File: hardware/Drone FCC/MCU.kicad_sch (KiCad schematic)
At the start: 11 parts, among them U3 STM32F746ZGTx

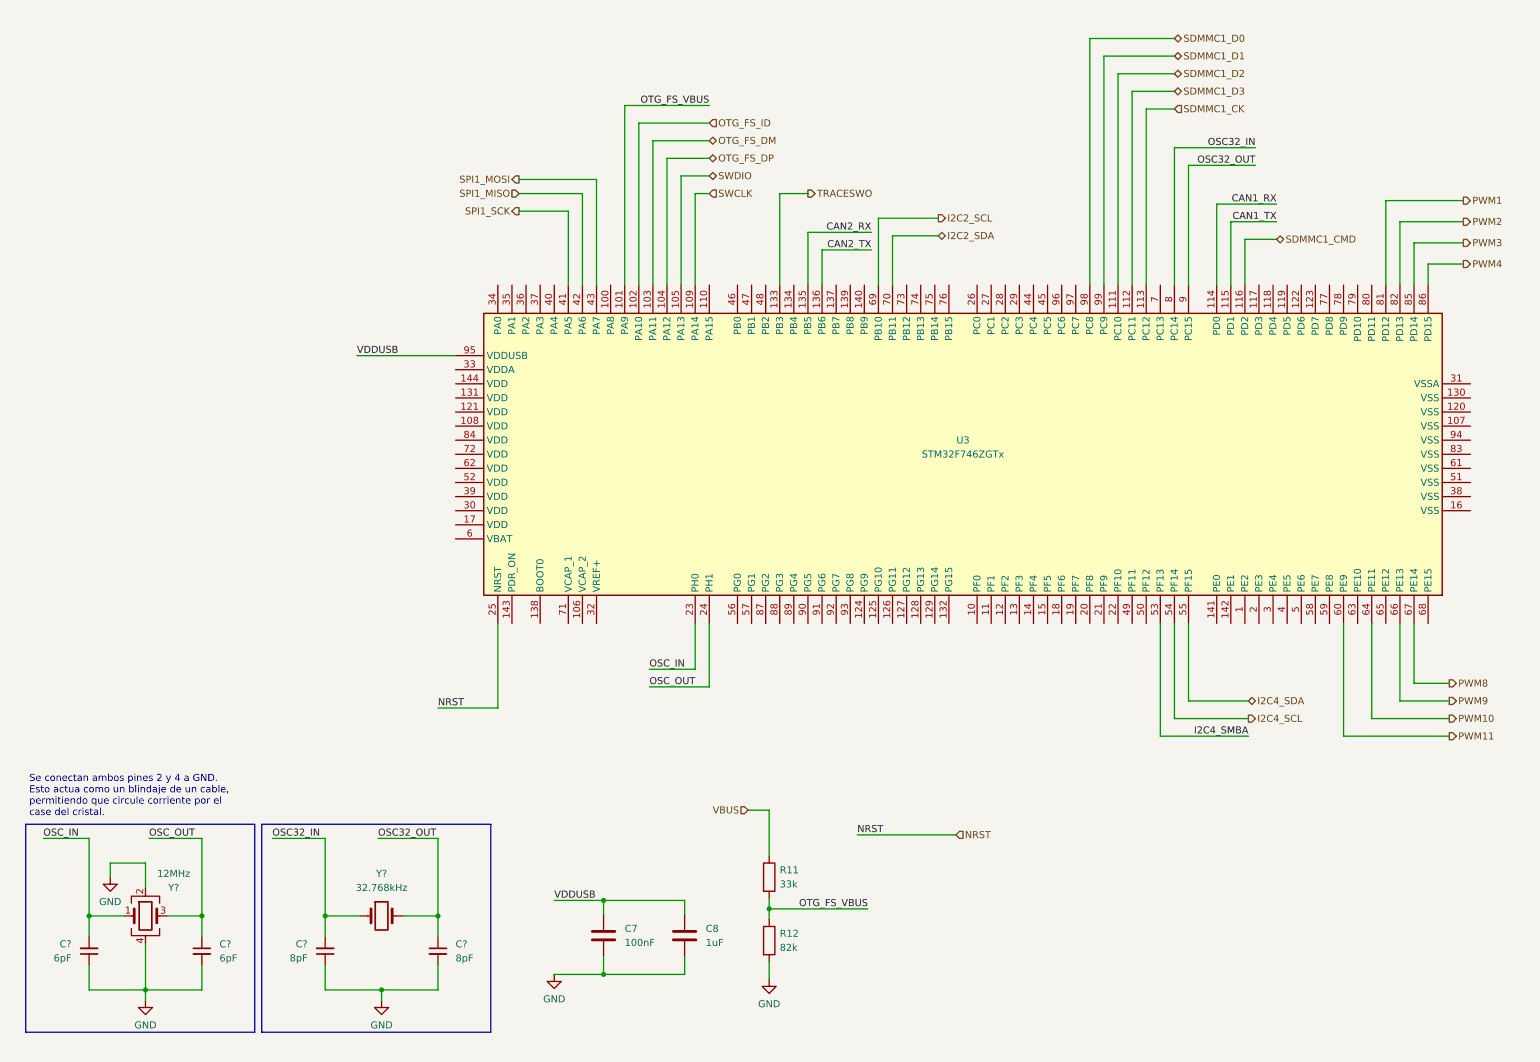
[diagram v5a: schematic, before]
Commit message: add CAN schematic
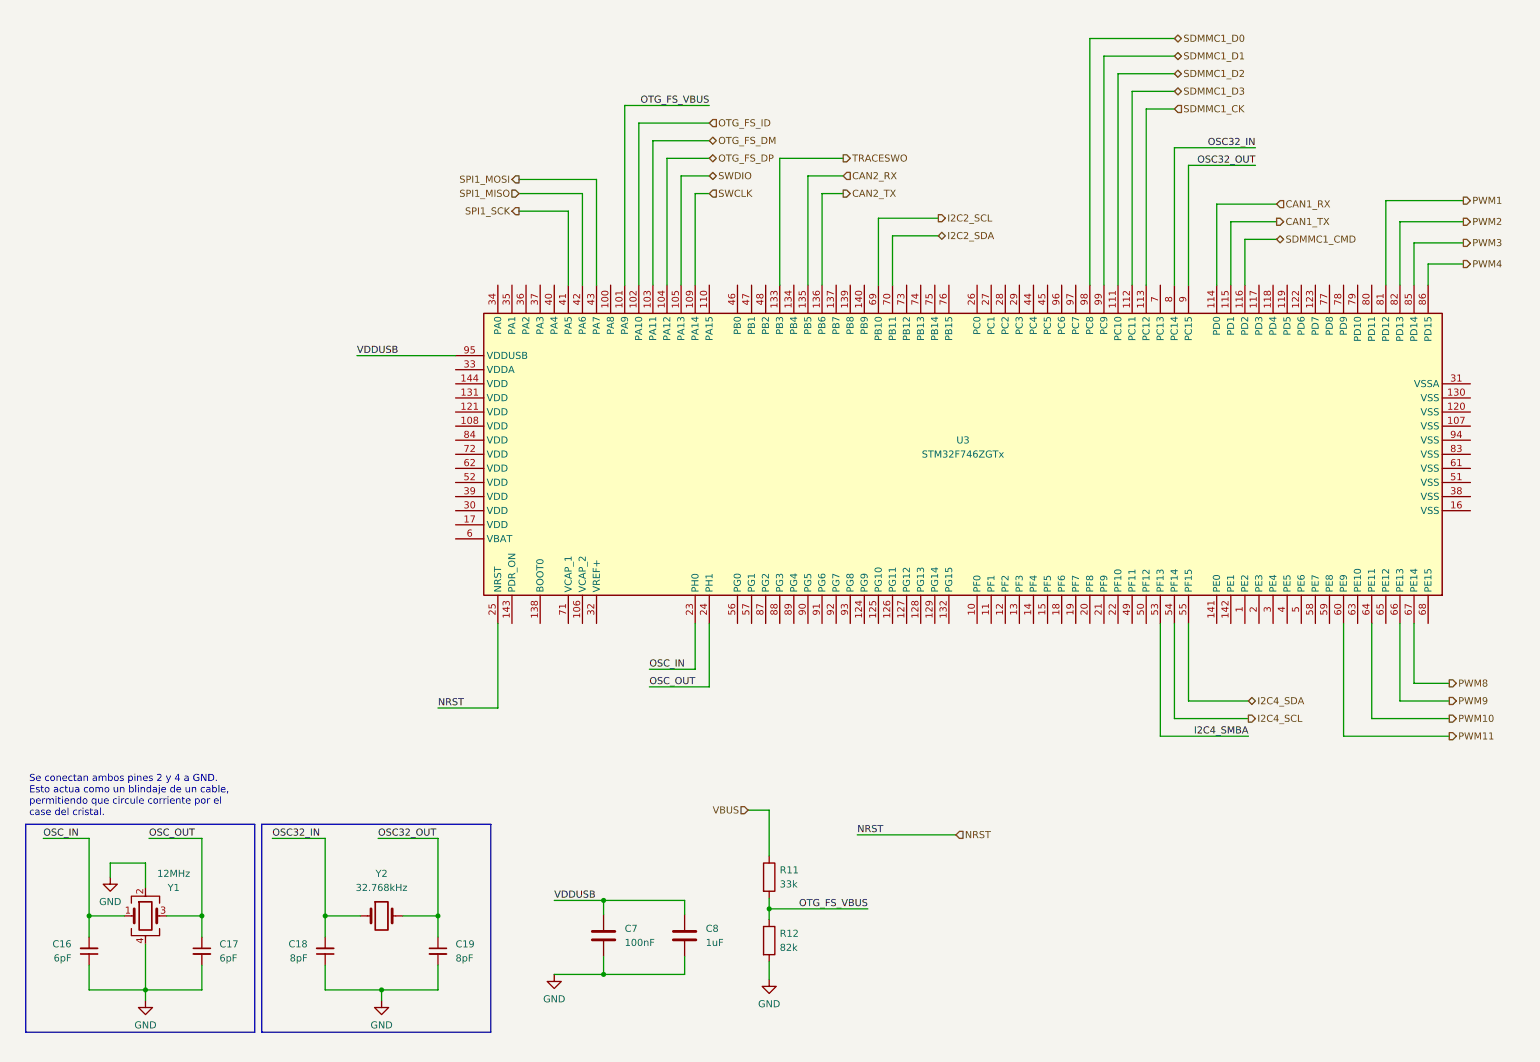
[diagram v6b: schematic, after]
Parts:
- gave numbers to parts that had none: 6
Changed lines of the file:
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@@
+    (stroke (width 0) (type default) (color 0 0 0 0))
+  )
+  (wire (pts (xy 148.59 39.37) (xy 148.59 62.23))
     (stroke (width 0) (type default) (color 0 0 0 0))
   )
@@
     (stroke (width 0) (type default) (color 0 0 0 0))
   )
-  (wire (pts (xy 153.67 52.705) (xy 165.1 52.705))
-    (stroke (width 0) (type default) (color 0 0 0 0))
-  )
   (wire (pts (xy 86.995 179.705) (xy 86.995 175.895))
     (stroke (width 0) (type default) (color 0 0 0 0))
@@
     (stroke (width 0) (type default) (color 0 0 0 0))
   )
-  (wire (pts (xy 148.59 45.72) (xy 153.67 45.72))
-    (stroke (width 0) (type default) (color 0 0 0 0))
-  )
   (wire (pts (xy 222.25 137.16) (xy 233.045 137.16))
     (stroke (width 0) (type default) (color 0 0 0 0))
@@
     (stroke (width 0) (type default) (color 0 0 0 0))
   )
-  (wire (pts (xy 148.59 62.23) (xy 148.59 45.72))
+  (wire (pts (xy 153.67 42.545) (xy 160.02 42.545))
     (stroke (width 0) (type default) (color 0 0 0 0))
   )
@@
     (stroke (width 0) (type default) (color 0 0 0 0))
   )
+  (wire (pts (xy 153.67 42.545) (xy 153.67 62.23))
+    (stroke (width 0) (type default) (color 0 0 0 0))
+  )
   (wire (pts (xy 125.095 131.445) (xy 133.35 131.445))
     (stroke (width 0) (type default) (color 0 0 0 0))
@@
     (stroke (width 0) (type default) (color 0 0 0 0))
   )
+  (wire (pts (xy 156.21 45.72) (xy 156.21 62.23))
+    (stroke (width 0) (type default) (color 0 0 0 0))
+  )
   (wire (pts (xy 73.025 175.895) (xy 66.675 175.895))
     (stroke (width 0) (type default) (color 0 0 0 0))
@@
     (stroke (width 0) (type default) (color 0 0 0 0))
   )
+  (wire (pts (xy 156.21 45.72) (xy 160.02 45.72))
+    (stroke (width 0) (type default) (color 0 0 0 0))
+  )
   (wire (pts (xy 217.17 143.51) (xy 217.17 123.19))
     (stroke (width 0) (type default) (color 0 0 0 0))
@@
     (stroke (width 0) (type default) (color 0 0 0 0))
   )
-  (wire (pts (xy 153.67 52.705) (xy 153.67 62.23))
-    (stroke (width 0) (type default) (color 0 0 0 0))
-  )
   (wire (pts (xy 207.01 20.955) (xy 207.01 62.23))
     (stroke (width 0) (type default) (color 0 0 0 0))
@@
     (stroke (width 0) (type default) (color 0 0 0 0))
   )
-  (wire (pts (xy 156.21 55.88) (xy 165.1 55.88))
+  (wire (pts (xy 148.59 39.37) (xy 160.02 39.37))
     (stroke (width 0) (type default) (color 0 0 0 0))
   )
@@
   )
   (polyline (pts (xy 53.975 196.85) (xy 53.975 159.385))
-    (stroke (width 0) (type default) (color 0 0 0 0))
-  )
-  (wire (pts (xy 156.21 55.88) (xy 156.21 62.23))
     (stroke (width 0) (type default) (color 0 0 0 0))
   )
@@
     (effects (font (size 1.27 1.27)) (justify right bottom))
   )
-  (label "CAN2_RX" (at 165.1 52.705 180)
-    (effects (font (size 1.27 1.27)) (justify right bottom))
-  )
-  (label "CAN2_TX" (at 165.1 55.88 180)
-    (effects (font (size 1.27 1.27)) (justify right bottom))
-  )
   (label "OSC_OUT" (at 125.095 134.62 0)
     (effects (font (size 1.27 1.27)) (justify left bottom))
@@
     (effects (font (size 1.27 1.27)) (justify left bottom))
   )
-  (label "CAN1_TX" (at 238.125 50.8 180)
-    (effects (font (size 1.27 1.27)) (justify right bottom))
-  )
-  (label "CAN1_RX" (at 238.125 47.625 180)
-    (effects (font (size 1.27 1.27)) (justify right bottom))
-  )
   (hierarchical_label "SDMMC1_D0" (shape bidirectional) (at 219.71 17.78 0)
     (effects (font (size 1.27 1.27)) (justify left))
@@
   )
   (hierarchical_label "OTG_FS_ID" (shape input) (at 135.89 33.02 0)
+    (effects (font (size 1.27 1.27)) (justify left))
+  )
+  (hierarchical_label "CAN1_TX" (shape output) (at 238.125 50.8 0)
     (effects (font (size 1.27 1.27)) (justify left))
   )
@@
     (effects (font (size 1.27 1.27)) (justify left))
   )
+  (hierarchical_label "CAN2_TX" (shape output) (at 160.02 45.72 0)
+    (effects (font (size 1.27 1.27)) (justify left))
+  )
   (hierarchical_label "PWM2" (shape output) (at 271.78 50.8 0)
     (effects (font (size 1.27 1.27)) (justify left))
@@
     (effects (font (size 1.27 1.27)) (justify left))
   )
+  (hierarchical_label "CAN2_RX" (shape input) (at 160.02 42.545 0)
+    (effects (font (size 1.27 1.27)) (justify left))
+  )
   (hierarchical_label "SDMMC1_CMD" (shape bidirectional) (at 238.125 53.975 0)
     (effects (font (size 1.27 1.27)) (justify left))
@@
     (effects (font (size 1.27 1.27)) (justify left))
   )
-  (hierarchical_label "TRACESWO" (shape output) (at 153.67 45.72 0)
+  (hierarchical_label "TRACESWO" (shape output) (at 160.02 39.37 0)
     (effects (font (size 1.27 1.27)) (justify left))
   )
@@
     (effects (font (size 1.27 1.27)) (justify left))
   )
+  (hierarchical_label "CAN1_RX" (shape input) (at 238.125 47.625 0)
+    (effects (font (size 1.27 1.27)) (justify left))
+  )
   (symbol (lib_id "power:GND") (at 107.95 186.436 0) (unit 1)
     (in_bom yes) (on_board yes) (fields_autoplaced)
@@
   (symbol (lib_id "Device:C_Small") (at 24.13 182.245 0) (mirror x) (unit 1)
     (in_bom yes) (on_board yes) (fields_autoplaced)
-    (property "Reference" "C?" (id 0) (at 20.955 180.9685 0)
+    (property "Reference" "C16" (id 0) (at 20.955 180.9685 0)
       (effects (font (size 1.27 1.27)) (justify right))
     )
@@
   (symbol (lib_id "Device:C_Small") (at 66.675 182.245 0) (mirror x) (unit 1)
     (in_bom yes) (on_board yes)
-    (property "Reference" "C?" (id 0) (at 63.5 180.9685 0)
+    (property "Reference" "C18" (id 0) (at 63.5 180.9685 0)
       (effects (font (size 1.27 1.27)) (justify right))
     )
@@
   (symbol (lib_id "Device:Crystal") (at 76.835 175.895 0) (unit 1)
     (in_bom yes) (on_board yes) (fields_autoplaced)
-    (property "Reference" "Y?" (id 0) (at 76.835 168.275 0))
+    (property "Reference" "Y2" (id 0) (at 76.835 168.275 0))
     (property "Value" "32.768kHz" (id 1) (at 76.835 170.815 0))
     (property "Footprint" "" (id 2) (at 76.835 175.895 0)
@@
   (symbol (lib_id "power:GND") (at 27.94 168.91 0) (unit 1)
     (in_bom yes) (on_board yes) (fields_autoplaced)
-    (property "Reference" "#PWR?" (id 0) (at 27.94 175.26 0)
+    (property "Reference" "#PWR0131" (id 0) (at 27.94 175.26 0)
       (effects (font (size 1.27 1.27)) hide)
     )
@@
   (symbol (lib_id "power:GND") (at 76.835 191.135 0) (unit 1)
     (in_bom yes) (on_board yes) (fields_autoplaced)
-    (property "Reference" "#PWR?" (id 0) (at 76.835 197.485 0)
+    (property "Reference" "#PWR0130" (id 0) (at 76.835 197.485 0)
       (effects (font (size 1.27 1.27)) hide)
     )
@@
   (symbol (lib_id "Device:Crystal_GND24") (at 34.29 175.895 0) (unit 1)
     (in_bom yes) (on_board yes)
-    (property "Reference" "Y?" (id 0) (at 39.37 170.815 0))
+    (property "Reference" "Y1" (id 0) (at 39.37 170.815 0))
     (property "Value" "12MHz" (id 1) (at 39.37 168.275 0))
     (property "Footprint" "" (id 2) (at 34.29 175.895 0)
@@
   (symbol (lib_id "power:GND") (at 34.29 191.135 0) (unit 1)
     (in_bom yes) (on_board yes) (fields_autoplaced)
-    (property "Reference" "#PWR?" (id 0) (at 34.29 197.485 0)
+    (property "Reference" "#PWR0132" (id 0) (at 34.29 197.485 0)
       (effects (font (size 1.27 1.27)) hide)
     )
@@
   (symbol (lib_id "Device:C_Small") (at 44.45 182.245 0) (unit 1)
     (in_bom yes) (on_board yes) (fields_autoplaced)
-    (property "Reference" "C?" (id 0) (at 47.625 180.9812 0)
+    (property "Reference" "C17" (id 0) (at 47.625 180.9812 0)
       (effects (font (size 1.27 1.27)) (justify left))
     )
@@
   (symbol (lib_id "Device:C_Small") (at 86.995 182.245 0) (unit 1)
     (in_bom yes) (on_board yes) (fields_autoplaced)
-    (property "Reference" "C?" (id 0) (at 90.17 180.9812 0)
-      (effects (font (size 1.27 1.27)) (justify left))
-    )
+    (property "Reference" "C19" (id 0) (at 90.17 180.9812 0)
+      (effects (font (size 1.27 1.27)) (justify left))
+    )

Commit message: rearranged FCC schematic
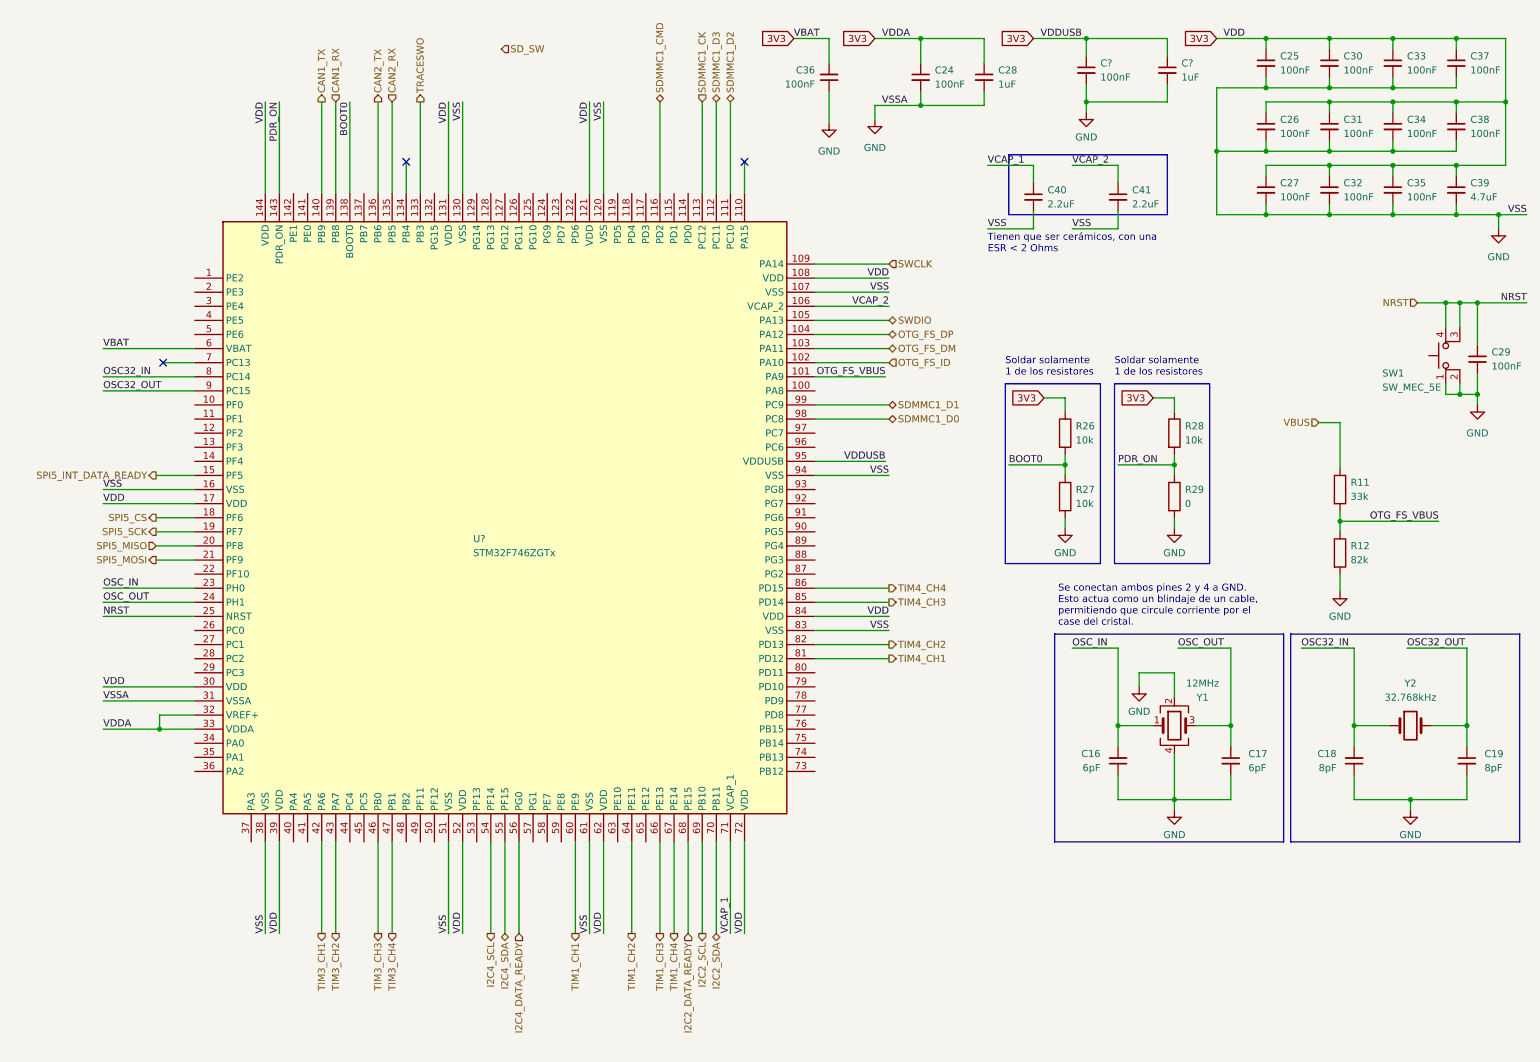
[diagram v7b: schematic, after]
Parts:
- removed C7: 100nF, symbol Device:C
- removed C8: 1uF, symbol Device:C
- removed U3: STM32F746ZGTx, Package_QFP:LQFP-144_20x20mm_P0.5mm, symbol MCU_ST_STM32F7:STM32F746ZGTx
- added C24, C25, C26, C27, C29, C30, C31, C32, C33, C34, C35, C36, C37, C38, C?: 100nF, symbol Device:C_Small
- added C28, C?: 1uF, symbol Device:C_Small
- added C39: 4.7uF, symbol Device:C_Small
- added C40, C41: 2.2uF, symbol Device:C_Small
- added R26, R27, R28: 10k, symbol Device:R
- added R29: 0, symbol Device:R
- added SW1: SW_MEC_5E, Button_Switch_SMD:SW_SPST_TL3305A, symbol Switch:SW_MEC_5E
- added U?: STM32F746ZGTx, Package_QFP:LQFP-144_20x20mm_P0.5mm, symbol STM32F746:STM32F746ZGTx
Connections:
- net CAN1_RX: now also U?.139 (PB8)
- net CAN1_TX: now also U?.140 (PB9)
- net CAN2_RX: now also U?.135 (PB5)
- net CAN2_TX: now also U?.136 (PB6)
- net GND: now also C24.2, C25.2, C26.2, C27.2, C28.2, C29.2, C30.2, C31.2, C32.2, C33.2, C34.2, C35.2, C36.1, C37.2, C38.2, C39.2, C40.2, C41.2, C?.2, C?.2, R27.2, R29.2, SW1.1, SW1.2, U?.107 (VSS), U?.120 (VSS), U?.130 (VSS), U?.16 (VSS), U?.31 (VSSA), U?.38 (VSS), U?.51 (VSS), U?.61 (VSS), U?.83 (VSS), U?.94 (VSS)
- net I2C2_SCL: now also U?.69 (PB10)
- net I2C2_SDA: now also U?.70 (PB11)
- net I2C4_SCL: now also U?.54 (PF14)
- net I2C4_SDA: now also U?.55 (PF15)
- net NRST: now also C29.1, SW1.3 (K), SW1.4 (A), U?.25 (NRST)
- net OSC32_IN: now also U?.8 (PC14)
- net OSC32_OUT: now also U?.9 (PC15)
- net OSC_IN: now also U?.23 (PH0)
- net OSC_OUT: now also U?.24 (PH1)
- net OTG_FS_DM: now also U?.103 (PA11)
- net OTG_FS_DP: now also U?.104 (PA12)
- net OTG_FS_ID: now also U?.102 (PA10)
- net OTG_FS_VBUS: now also U?.101 (PA9)
- net SDMMC1_CK: now also U?.113 (PC12)
- net SDMMC1_CMD: now also U?.116 (PD2)
- net SDMMC1_D0: now also U?.98 (PC8)
- net SDMMC1_D1: now also U?.99 (PC9)
- net SDMMC1_D2: now also U?.111 (PC10)
- net SDMMC1_D3: now also U?.112 (PC11)
- net SWCLK: now also U?.109 (PA14)
- net SWDIO: now also U?.105 (PA13)
- net TRACESWO: now also U?.133 (PB3)
- new net 3V3: C24.1, C25.1, C26.1, C27.1, C28.1, C30.1, C31.1, C32.1, C33.1, C34.1, C35.1, C36.2, C37.1, C38.1, C39.1, C?.1, C?.1, R26.1, R28.1, U?.108 (VDD), U?.121 (VDD), U?.131 (VDD), U?.144 (VDD), U?.17 (VDD), U?.30 (VDD), U?.32 (VREF+), U?.33 (VDDA), U?.39 (VDD), U?.52 (VDD), U?.6 (VBAT), U?.62 (VDD), U?.72 (VDD), U?.84 (VDD), U?.95 (VDDUSB)
- new net BOOT0: R26.2, R27.1, U?.138 (BOOT0)
- new net I2C2_DATA_READY: U?.68 (PE15)
- new net I2C4_DATA_READY: U?.56 (PG0)
- new net PDR_ON: R28.2, R29.1, U?.143 (PDR_ON)
- new net SPI5_CS: U?.18 (PF6)
- new net SPI5_INT_DATA_READY: U?.15 (PF5)
- new net SPI5_MISO: U?.20 (PF8)
- new net SPI5_MOSI: U?.21 (PF9)
- new net SPI5_SCK: U?.19 (PF7)
- new net TIM1_CH1: U?.60 (PE9)
- new net TIM1_CH2: U?.64 (PE11)
- new net TIM1_CH3: U?.66 (PE13)
- new net TIM1_CH4: U?.67 (PE14)
- new net TIM3_CH1: U?.42 (PA6)
- new net TIM3_CH2: U?.43 (PA7)
- new net TIM3_CH3: U?.46 (PB0)
- new net TIM3_CH4: U?.47 (PB1)
- new net TIM4_CH1: U?.81 (PD12)
- new net TIM4_CH2: U?.82 (PD13)
- new net TIM4_CH3: U?.85 (PD14)
- new net TIM4_CH4: U?.86 (PD15)
- new net VCAP_1: C40.1, U?.71 (VCAP_1)
- new net VCAP_2: C41.1, U?.106 (VCAP_2)
- no-connect marks 0 -> 3
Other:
- note added: "Soldar solamente 1 de los resistores"
- note added: "Tienen que ser cerámicos, con una ESR < 2 Ohms"
- moved on the sheet: C16, C17, C18, C19, R11, R12, Y1, Y2
